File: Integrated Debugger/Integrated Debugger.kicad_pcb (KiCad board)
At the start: 4 copper layers, 36.8 x 16.4 mm, 58 parts, among them J1 B2B GT-B0353FSV06-08B0201, J2 USB_C (PC <-> Host), J3 FPC socket 10P, J4 20021521-00010T1LF, J5 PWR, Q1 NMOS DMN2991UDA-7B, SW1 BOOT, SW2 RESET, SW3 Solar Override, SW4 Target Override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

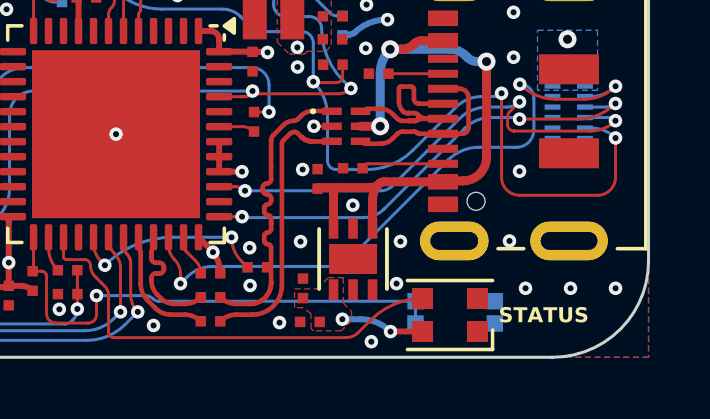
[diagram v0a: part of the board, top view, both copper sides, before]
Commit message: feat: swap debugger rgb led part
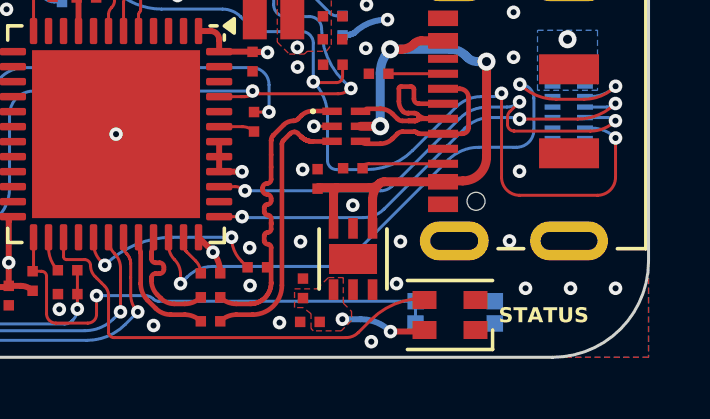
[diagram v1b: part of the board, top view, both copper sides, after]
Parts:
- D1: footprint Picoballoon ICs:WS2812B-2020 -> Picoballoon ICs:WS2812B-2121

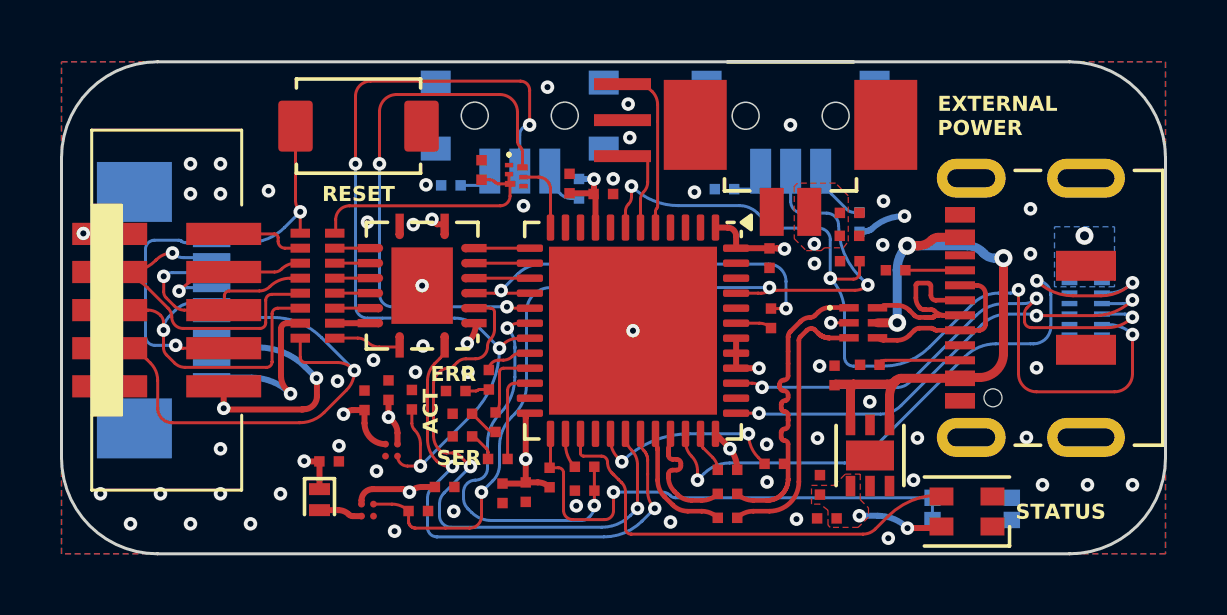
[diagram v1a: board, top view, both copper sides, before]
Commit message: Change diode
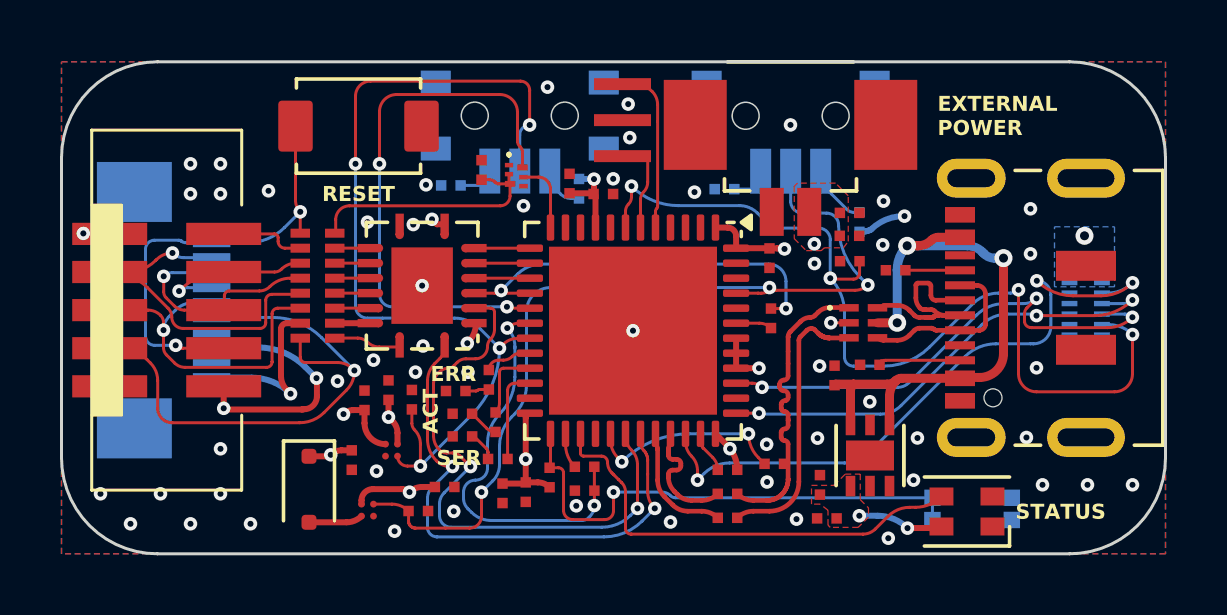
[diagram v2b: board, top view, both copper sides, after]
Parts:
- D1: value WS2812B-2020 -> XL-2121RGBC-WS2812B
- D5: footprint Picoballoon Passives:Diode SOD-882 -> Picoballoon Passives:Diode SOD-323F
- moved C13 0.76 mm to (153.4, 90.9), turned to -90 degrees
- moved D5 0.49 mm to (151.9, 91.8)
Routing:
- net V_SOLAR: track 13.7 -> 14.4 mm
- net GND: vias 56 -> 54

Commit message: feat: fix debugger bugs & impl. auxiliary power - 869b0p9f3
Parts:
- removed D5: CTS520,L3F(T, Picoballoon Passives:Diode SOD-323F
- added C17: 100nF, Picoballoon Passives:Capacitor 0201, F.Cu at (151.6, 93.3)
- added Q2: Generic N-MOSFET, PCM_Picoballoon ICs:PICOSTAR-3, B.Cu at (152.5, 79.5)
- added R20: 4.7kΩ, Picoballoon Passives:Resistor 0201, F.Cu at (161.5, 92.9)
- added R21: 10kΩ, Picoballoon Passives:Resistor 0201, F.Cu at (161.1, 91.1)
- SW3: value Solar Override -> Auxiliary Override
- moved R12 9.61 mm to (151.5, 92.5)
- moved R11 9.61 mm to (151.5, 91.7)
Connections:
- net /MCU/SOL_EN renamed /MCU/AUX_EN
- C13 pad 1: V_SOLAR -> V_AUX
- C15 pad 1: V_TARGET -> V_AUX
- C16 pad 1: V_TARGET -> V_AUX
- C9 pad 1: +5V -> +3.3V
- J3 pad 3: V_SOLAR -> V_AUX
- J4 pad 10: V_SOLAR -> V_AUX
- J5 pad 1: V_TARGET -> V_AUX
- R11 pad 1: /MCU/VBUS -> V_TARGET
- SW4 pad 2: /MCU/TARGET_EN -> Net-(Q2-G)
- U5 pad A1: /Power/V_SOLAR_UNFILT -> V_AUX
- U5 pad A2: +5V -> +3.3V
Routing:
- net V_AUX: track 0.00 -> 53.5 mm, vias 0 -> 4
- net V_TARGET: track 50.4 -> 24.5 mm, vias 4 -> 3
- net V_SOLAR: track 14.4 -> 0.00 mm, vias 3 -> 0
- net Net-(Q2-G): track 0.00 -> 10.3 mm, vias 0 -> 2
- net /MCU/TARGET_EN: track 29.9 -> 20.5 mm, vias 4 -> 2
- net +5V: track 47.2 -> 41.1 mm
- net Net-(Q2-S): track 1.69 -> 6.68 mm
- net +3.3V: track 20.2 -> 23.0 mm, vias 12 -> 13
- net /Power/V_SOLAR_UNFILT: track 1.80 -> 0.00 mm
- net /MCU/VBUS: track 1.18 -> 2.86 mm
- net /Target/tTMS: track 5.97 -> 7.56 mm
- net Net-(SW1-B): track 17.0 -> 15.6 mm
- net /MCU/LEDX: track 15.7 -> 14.7 mm
- added copper zone on F.Cu, net V_AUX
- removed copper zone on F.Cu, net V_TARGET
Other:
- board text added: "AUX POWER"
- board text removed: "SOLAR POWER"

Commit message: Prepare for production
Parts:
- moved R16 1.05 mm to (171.3, 82.6), turned to 180 degrees
- moved C13 0.50 mm to (153.0, 91.2), turned to 0 degrees
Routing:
- net /Target/tTMS: track 7.56 -> 5.97 mm
- net /MCU/LEDX: track 14.7 -> 16.1 mm
- net +3.3V: track 23.0 -> 21.7 mm
- net Net-(R16-Pad2): track 2.11 -> 2.99 mm
- net +5V: track 41.1 -> 40.3 mm
- net GND: vias 54 -> 55
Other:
- board text added: "V1.1"
- board text removed: "V1.0"

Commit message: fix(debugger): relpace picostar 0.4 with 0.65 variant
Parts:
- Q2: footprint PCM_Picoballoon ICs:PICOSTAR-3 -> Picoballoon ICs:PICOSTAR-3_0.65

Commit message: Debugger 1.1.2 production files
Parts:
- RN1: footprint Picoballoon Passives:Resistor Pack YC248-JR-07100RL -> Picoballoon Passives:Resistor 0402x8
- U2: footprint Picoballoon ICs:QFN-48-1EP_7x7mm_P0.5mm_EP5.6x5.6mm -> Picoballoon ICs:QFN-48 7x7mm
- U3: footprint Picoballoon ICs:Texas_RGY_R-PVQFN-N16_EP2.05x2.55mm -> Picoballoon ICs:PVQFN-N16
- Y1: footprint Picoballoon Passives:Crystal CSTNE8M00GH5C000R0 -> Picoballoon Passives:Crystal 3213-3P
- turned U2 to 90 degrees

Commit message: Update assembly
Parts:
- moved J5 2.90 mm to (168.0, 82.6)
- moved J2 1.15 mm to (177.8, 85.8)
- turned U1 to 90 degrees
- turned U3 to 90 degrees

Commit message: Update component models
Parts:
- moved J5 2.90 mm to (168.0, 79.7)
